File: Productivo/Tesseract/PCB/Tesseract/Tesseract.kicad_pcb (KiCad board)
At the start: 2 copper layers, 100 x 100 mm, 81 parts, among them J1 V-coil1, J10 RTC, J12 V-coil2, J13 Conn_01x06_Pin RTC, J14 AUX, J15 READER, J16 jumpers salida, J17 RFW26, J19 OUT+, J2 IN+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

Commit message: ruteo pcb
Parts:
- moved R13 16.5 mm to (115.2, 98.5)
- moved R2 12.5 mm to (108.5, 98.5)
- moved R24 9.70 mm to (115.5, 72.0)
- moved R11 8.53 mm to (101.8, 98.5)
- moved R18 7.72 mm to (110.8, 72.0)
- moved R5 6.53 mm to (106.0, 72.0)
- moved R15 4.83 mm to (95.1, 98.5)
- moved R22 4.79 mm to (101.3, 72.0)
- moved R20 3.06 mm to (96.5, 72.0)
- moved R23 2.29 mm to (81.7, 98.5)
- moved R21 1.17 mm to (88.4, 98.5)
- moved R7 1.04 mm to (87.1, 72.0)
- moved R8 1.04 mm to (91.8, 72.0)
- moved C5 0.80 mm to (82.3, 72.0)
- moved R10 0.20 mm to (75.0, 98.5)
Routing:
- net Net-(D17-A): track 71.1 -> 264.3 mm, vias 2 -> 4
- net Net-(Q3-B): track 33.6 -> 205.8 mm, vias 0 -> 6
- net Net-(Q1-B): track 80.4 -> 211.0 mm, vias 0 -> 2
- net Net-(D5-A): track 48.6 -> 157.9 mm, vias 2 -> 4
- net GND: track 433.2 -> 532.0 mm, vias 2 -> 4
- net Net-(Q4-B): track 54.3 -> 130.5 mm, vias 2 -> 4
- net SDA: track 72.7 -> 146.1 mm
- net Net-(U3-EN): track 6.75 -> 76.3 mm, vias 0 -> 4
- net GPIO0: track 79.2 -> 144.3 mm, vias 3 -> 6
- net Net-(Q2-B): track 50.7 -> 107.7 mm
- net +5V: track 166.2 -> 213.7 mm, vias 4 -> 3
- net 12VOUT: track 112.8 -> 150.3 mm, vias 1 -> 0
- net Net-(Q5-B): track 45.5 -> 71.7 mm
- net +12V: track 187.9 -> 213.8 mm
- net GPIO5: track 5.90 -> 22.6 mm
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
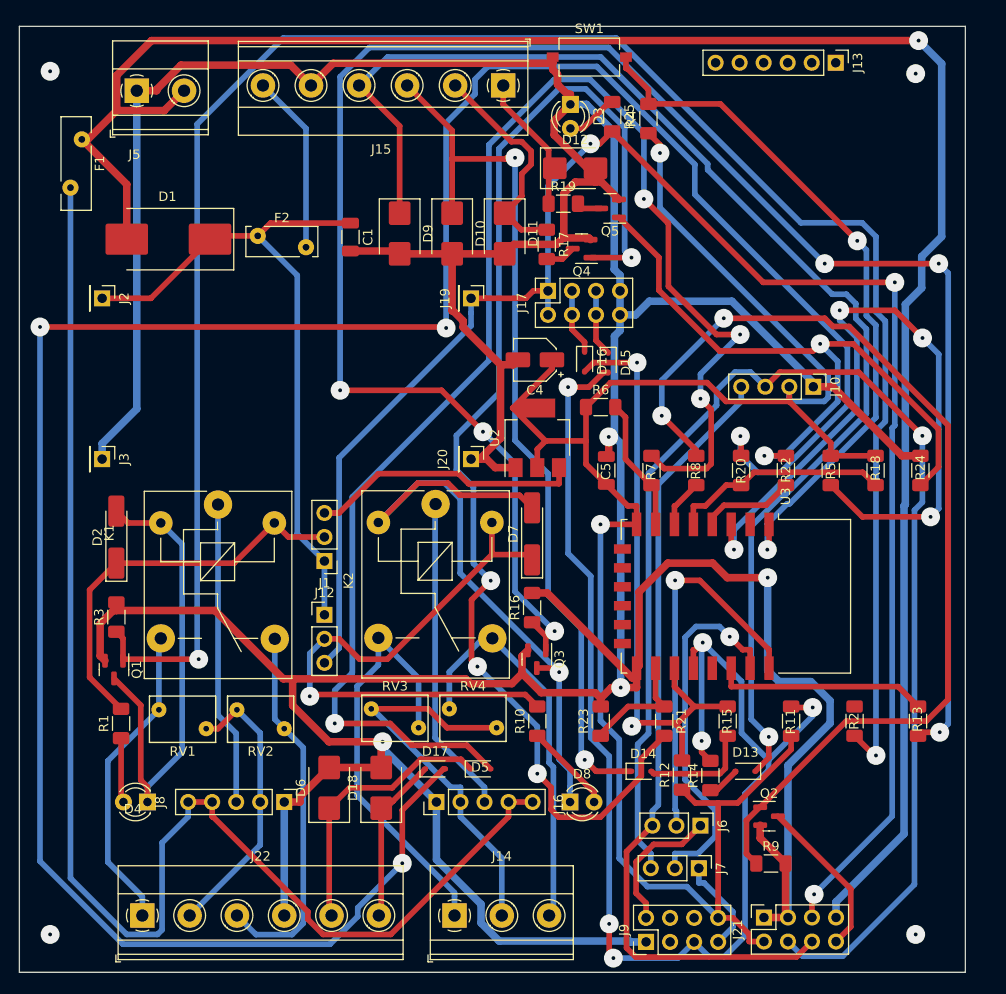
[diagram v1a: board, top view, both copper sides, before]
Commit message: ajuste 2 capaz tesseract
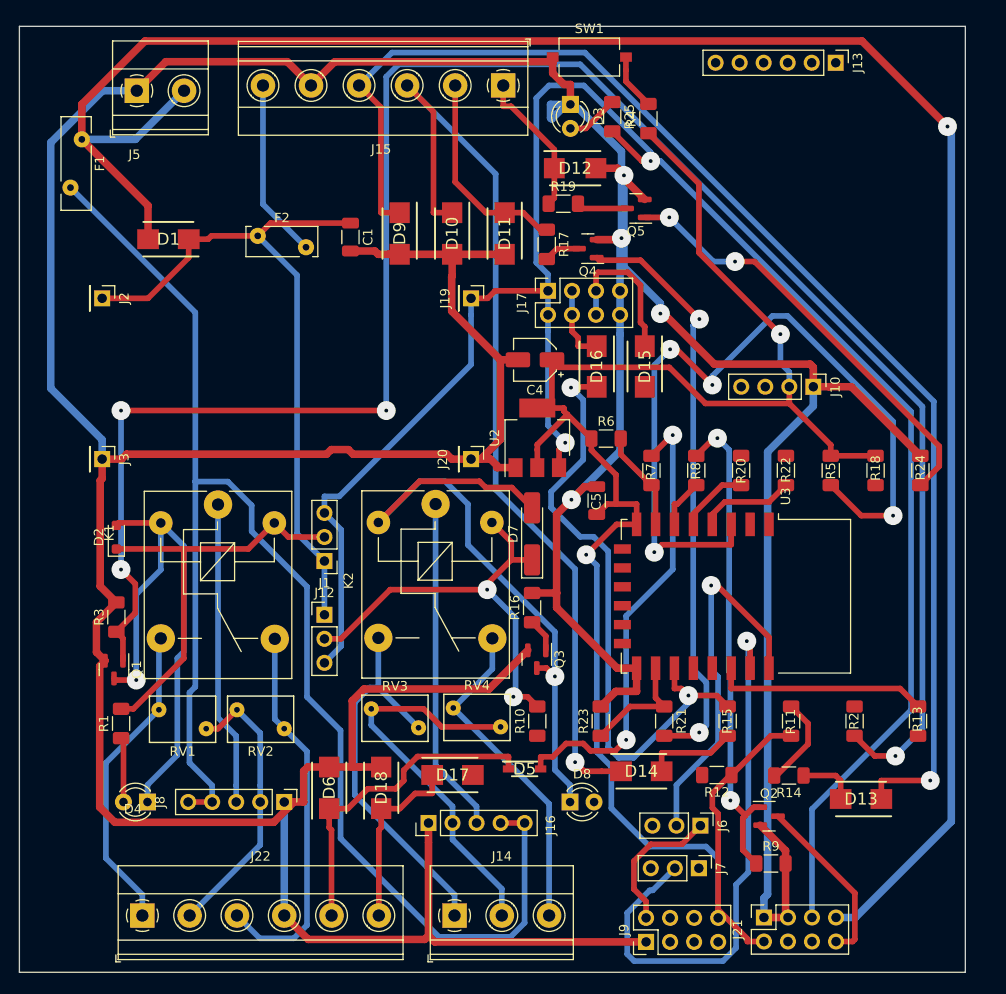
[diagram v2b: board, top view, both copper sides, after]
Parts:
- D1: footprint Diode_SMD:D_SMC_Handsoldering -> modelos:DIOM5336X320N
- D10, D11, D12, D18, D6, D9: footprint Diode_SMD:D_SMB -> modelos:DIOM5436X265N
- D13, D14, D15, D16, D17: footprint Diode_SMD:D_SOD-323 -> modelos:DIOM5336X320N
- D2: footprint Diode_SMD:D_MiniMELF_Handsoldering -> Diode_SMD:D_SOD-323_HandSoldering
- D5: footprint Diode_SMD:D_SOD-323 -> modelos:SOD3716X145N
- moved D13 12.6 mm to (109.2, 106.7)
- moved R14 8.30 mm to (101.6, 104.2), turned to 180 degrees
- moved D5 4.66 mm to (73.7, 103.5)
- moved D15 3.88 mm to (86.4, 61.0)
- moved R12 3.68 mm to (94.0, 104.2), turned to 180 degrees
- moved R6 3.38 mm to (82.3, 68.6)
- moved C5 3.34 mm to (81.3, 75.1)
- moved Q5 2.73 mm to (85.4, 44.2)
- moved J16 2.37 mm to (63.5, 109.2)
- moved D17 1.95 mm to (66.0, 104.1)
- moved D16 1.38 mm to (81.3, 61.0)
- moved Q4 0.66 mm to (80.3, 48.5)
- moved RV4 0.43 mm to (71.1, 99.1)
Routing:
- net Net-(D17-A): track 264.3 -> 0.00 mm, vias 4 -> 0
- net Net-(Q3-B): track 205.8 -> 3.56 mm, vias 6 -> 0
- net SDA: track 146.1 -> 0.00 mm, vias 1 -> 0
- net GPIO0: track 144.3 -> 9.67 mm, vias 6 -> 0
- net Net-(D5-A): track 157.9 -> 49.1 mm, vias 4 -> 2
- net SCL: track 85.0 -> 0.00 mm
- net Net-(U3-~{RST}): track 75.2 -> 5.93 mm, vias 2 -> 0
- net Net-(Q4-B): track 130.5 -> 62.3 mm, vias 4 -> 2
- net Net-(Q2-B): track 107.7 -> 51.9 mm
- net GND: track 532.0 -> 575.7 mm
- net Net-(Q5-B): track 71.7 -> 46.1 mm
- net SDA/RX: track 39.2 -> 59.8 mm
- net Net-(D7-K): track 62.4 -> 46.2 mm, vias 1 -> 2
- net GPIO14: track 23.2 -> 7.42 mm
- net +3.3V: track 203.2 -> 192.6 mm
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
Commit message: reacomodado de componentes
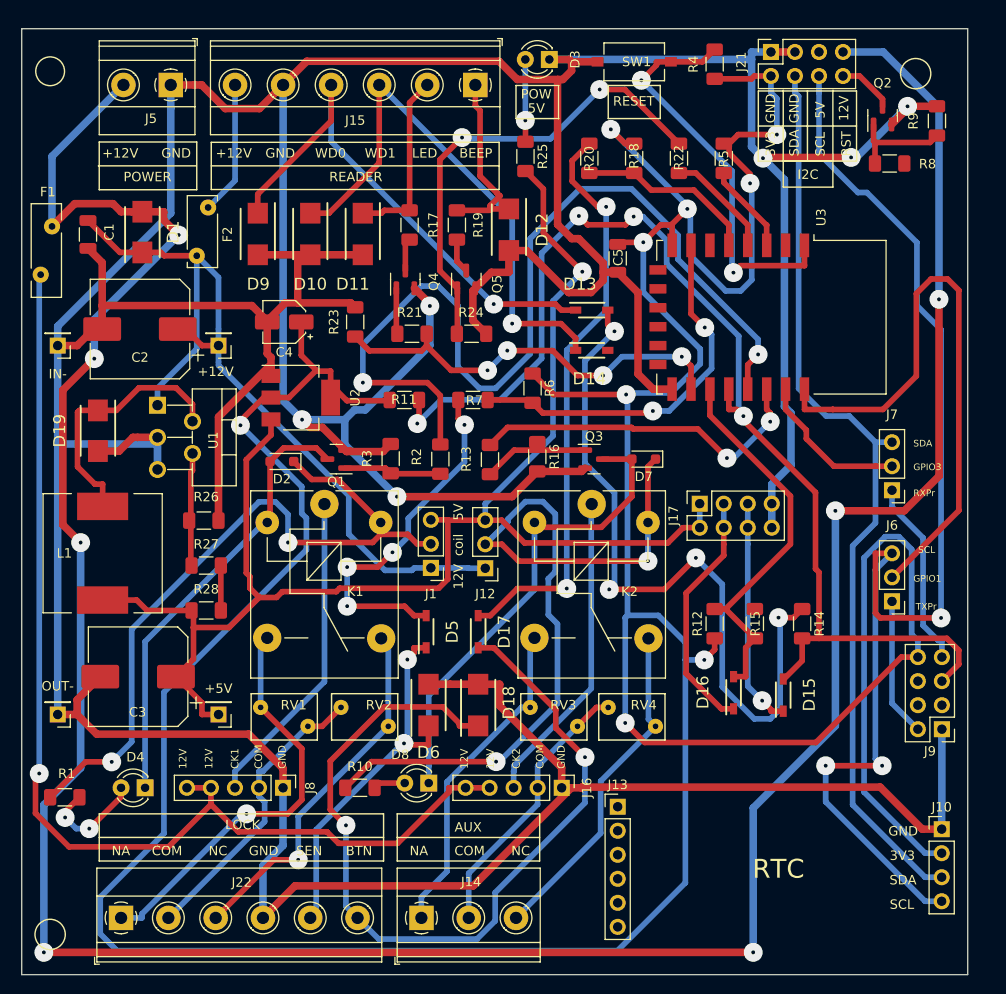
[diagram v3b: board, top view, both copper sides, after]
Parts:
- added C2: 220uF/35V, Capacitor_SMD:CP_Elec_10x10, F.Cu at (33.0, 57.0)
- added C3: 220uF/35V, Capacitor_SMD:CP_Elec_10x10, F.Cu at (32.8, 93.8)
- added D19: SS34, modelos:DIOM5336X320N, F.Cu at (28.6, 67.8)
- added L1: 33 uH/3.5A, Inductor_SMD:L_12x12mm_H8mm, F.Cu at (29.1, 80.7)
- added R26: 4.7K, Resistor_SMD:R_1206_3216Metric_Pad1.30x1.75mm_HandSolder, F.Cu at (39.8, 77.2)
- added R27: 4.7K, Resistor_SMD:R_1206_3216Metric_Pad1.30x1.75mm_HandSolder, F.Cu at (40.0, 82.0)
- added R28: 10K, Resistor_SMD:R_1206_3216Metric_Pad1.30x1.75mm_HandSolder, F.Cu at (40.0, 86.8)
- added U1: LM2596S-5, Package_TO_SOT_THT:TO-220-5_P3.4x3.7mm_StaggerOdd_Lead3.8mm_Vertical, F.Cu at (34.9, 65.0)
- D13, D14, D15, D16, D17: footprint modelos:DIOM5336X320N -> modelos:SOD3716X145N
- D7: footprint Diode_SMD:D_MiniMELF_Handsoldering -> Diode_SMD:D_SOD-323_HandSoldering
- moved J21 91.5 mm to (99.7, 27.7)
- moved J13 82.0 mm to (83.5, 107.5), turned to 0 degrees
- moved R9 80.4 mm to (117.2, 35.0), turned to 90 degrees
- moved Q2 75.0 mm to (111.5, 34.4), turned to 90 degrees
- moved D13 59.0 mm to (80.8, 55.0), turned to 0 degrees
- moved R11 53.1 mm to (61.0, 64.5), turned to 0 degrees
- moved R13 53.0 mm to (70.0, 70.8)
- moved R2 51.8 mm to (64.8, 70.8)
- moved +5V 51.5 mm to (41.3, 97.8), turned to 180 degrees
- moved OUT- 51.4 mm to (24.3, 97.8), turned to 180 degrees
- moved R24 49.6 mm to (68.0, 57.5), turned to 0 degrees
- moved R23 49.5 mm to (55.8, 56.2)
- moved R21 48.9 mm to (61.8, 57.5), turned to 180 degrees
- moved J10 48.7 mm to (117.8, 109.9), turned to 0 degrees
- moved J7 44.9 mm to (112.5, 74.0), turned to 180 degrees
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- renumbered J2 to +12V, J19 to +5V, J3 to IN-, J20 to OUT-
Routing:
- net +3.3V: track 192.6 -> 429.6 mm, vias 2 -> 9
- net Net-(Q1-B): track 207.1 -> 10.3 mm, vias 4 -> 0
- net SCL: track 0.00 -> 128.3 mm, vias 0 -> 3
- net GPIO0: track 9.67 -> 125.3 mm, vias 0 -> 4
- net GPIO4: track 0.00 -> 100.2 mm, vias 0 -> 2
- net SDA: track 0.00 -> 97.3 mm
- net +12V: track 218.2 -> 306.9 mm, vias 1 -> 7
- net D0: track 141.2 -> 56.0 mm
- net GND: track 575.7 -> 659.0 mm, vias 4 -> 6
- net Net-(U3-EN): track 84.0 -> 9.55 mm, vias 4 -> 0
- net Net-(D13-A): track 6.09 -> 78.5 mm, vias 0 -> 4
- net BTN: track 19.4 -> 91.5 mm, vias 0 -> 2
- net Net-(D17-A): track 0.00 -> 62.1 mm, vias 0 -> 2
- net +5V: track 214.6 -> 156.6 mm, vias 2 -> 1
- net Net-(Q4-B): track 62.3 -> 4.85 mm, vias 2 -> 0
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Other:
- board text added: "+12V"
- board text added: "12V"
- board text added: "3V3"
- board text added: "5V"
- board text added: "AUX"
- board text added: "BEEP"
- board text added: "BTN"
- board text added: "CK1"
- board text added: "CK2"
- board text added: "COM"
- board text added: "GND"
- board text added: "GPIO1"
- board text added: "GPIO3"
- board text added: "I2C"
- board text added: "LED"
- board text added: "LOCK"
- board text added: "NA"
- board text added: "NC"
- board text added: "POW"
- board text added: "POWER"
- board text added: "READER"
- board text added: "RESET"
- board text added: "RST"
- board text added: "RTC"
- board text added: "RXPr"
- board text added: "SCL"
- board text added: "SDA"
- board text added: "SEN"
- board text added: "TXPr"
- board text added: "WD0"
- board text added: "WD1"
- board text added: "coil"

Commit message: Cambios tesseract EMI
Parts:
- moved D13 51.5 mm to (108.2, 98.5), turned to 90 degrees
- moved D14 41.3 mm to (92.0, 99.0), turned to 90 degrees
- moved R12 12.0 mm to (99.8, 98.5)
- moved R6 10.6 mm to (82.2, 56.0)
- moved D16 10.4 mm to (91.8, 85.8), turned to -90 degrees
- moved D15 10.4 mm to (97.2, 86.0), turned to -90 degrees
- moved J7 8.61 mm to (106.8, 80.4)
- moved D7 7.65 mm to (81.5, 64.8), turned to -90 degrees
- moved R15 6.63 mm to (93.0, 92.5), turned to 0 degrees
- moved J6 5.42 mm to (114.5, 80.8)
- moved R14 5.04 mm to (99.8, 92.0), turned to 90 degrees
- moved U3 3.72 mm to (102.5, 58.2)
- moved R5 3.54 mm to (95.5, 35.5)
- moved R2 1.35 mm to (64.2, 72.0)
- moved C5 1.27 mm to (82.2, 49.8)
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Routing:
- net +3.3V: track 429.6 -> 240.7 mm, vias 9 -> 1
- net +12V: track 306.9 -> 164.5 mm, vias 7 -> 3
- net D1: track 57.4 -> 138.0 mm
- net +5V: track 156.6 -> 227.6 mm
- net Net-(D13-A): track 78.5 -> 9.85 mm, vias 4 -> 0
- net D0: track 56.0 -> 122.8 mm, vias 1 -> 2
- net GPIO4: track 100.2 -> 45.2 mm, vias 2 -> 0
- net Net-(D17-A): track 62.1 -> 115.9 mm
- net GPIO15: track 44.3 -> 95.4 mm, vias 4 -> 2
- net SCL/TX: track 63.1 -> 15.9 mm
- net BTN: track 91.5 -> 46.8 mm, vias 2 -> 0
- net SCL: track 128.3 -> 93.8 mm, vias 3 -> 1
- net GPIO12: track 0.00 -> 30.2 mm, vias 0 -> 2
- net GPIO2: track 40.9 -> 58.4 mm, vias 0 -> 2
- net Net-(Q4-B): track 4.85 -> 22.0 mm
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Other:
- board text added: "RFW26"
